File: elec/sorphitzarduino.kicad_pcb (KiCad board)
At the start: 2 copper layers, 135.9 x 67.3 mm, 13 parts, among them J1 9V_BATT, J2 SWITCH, J3 AUDIO_JACK, U1 ARDUINO_MICRO_SHIELD

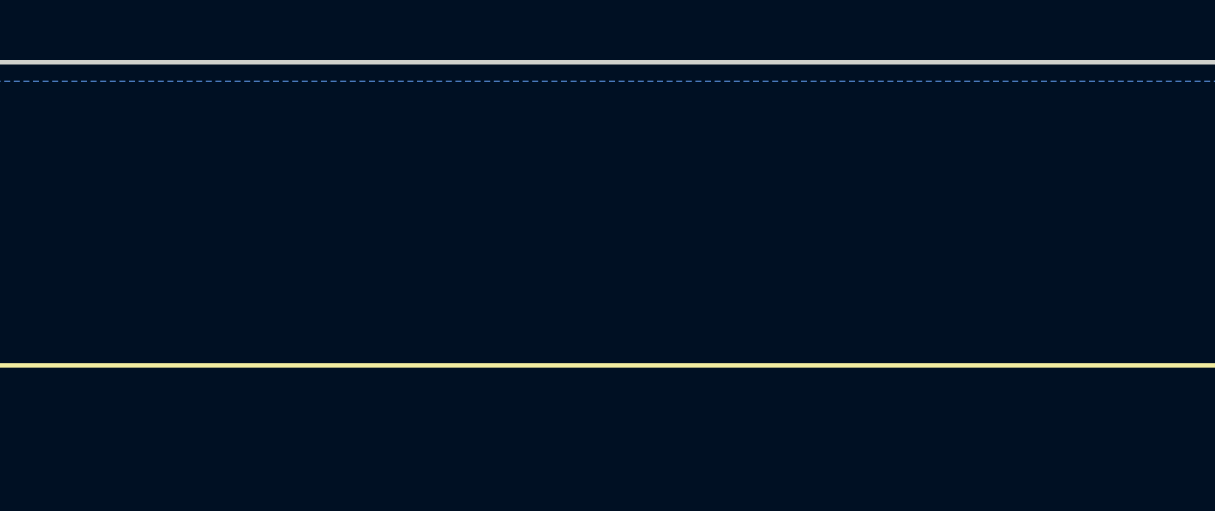
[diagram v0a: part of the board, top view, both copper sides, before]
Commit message: Updating SVG output to be only board
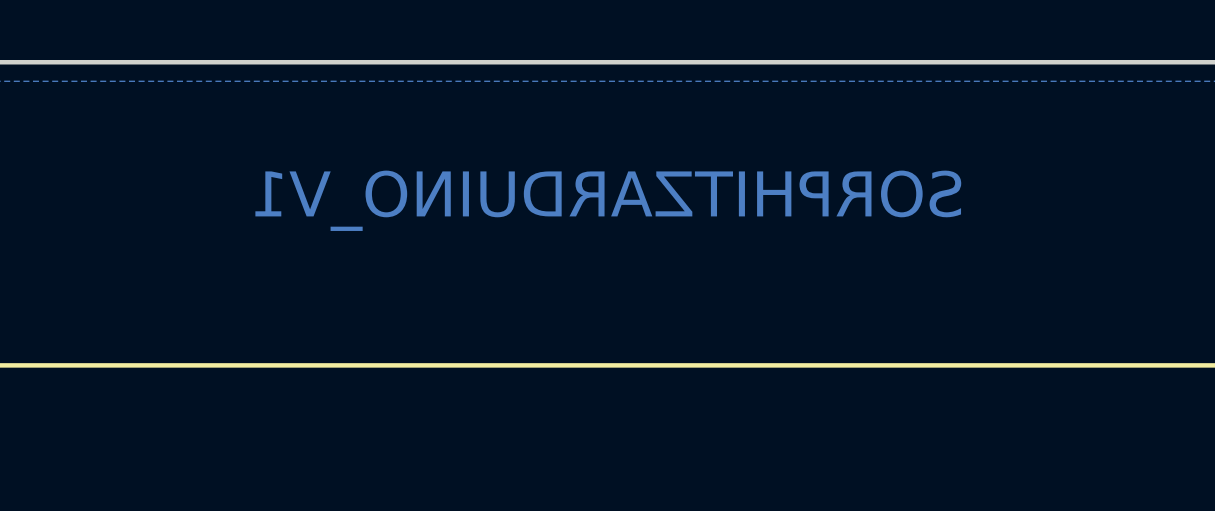
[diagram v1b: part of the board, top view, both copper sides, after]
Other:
- board text added: "SORPHITZARDUINO_V1"
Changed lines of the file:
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@@
     (area 111.684999 24.689999 247.725001 92.150001)
     (thickness 1.6)
-    (drawings 10)
+    (drawings 11)
     (tracks 90)
     (zones 0)
@@
     (pad "" thru_hole circle (at 31.4 -4.2) (size 3 3) (drill 1.7) (layers *.Cu *.Mask F.SilkS))
   )
+  (gr_text SORPHITZARDUINO_V1 (at 200.025 29.21) (layer B.Cu)
+    (effects (font (size 1.5 1.5) (thickness 0.3)) (justify mirror))
+  )
   (dimension 12.065 (width 0.3) (layer Margin)
